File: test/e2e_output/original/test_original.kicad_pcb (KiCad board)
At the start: 2 copper layers, 3 parts, among them U1 CP_Radial_D25.0mm_P10.00mm_Sn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, U2 R_Axial_DIN0207_L6.3mm_D2.5mm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, U3 R_Axial_DIN0207_L6.3mm_D2.5mm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

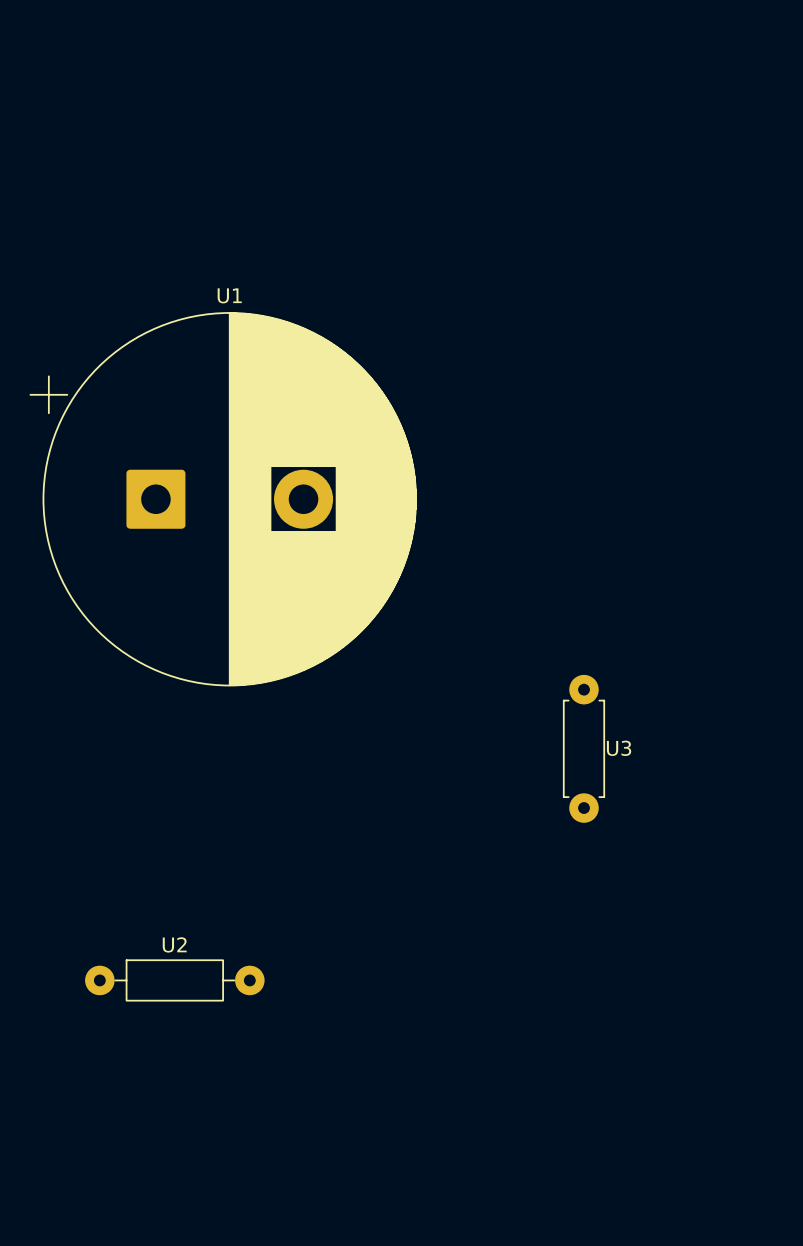
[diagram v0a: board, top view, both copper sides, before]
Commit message: fix: schematic router - pin_map mapping + rotation formula alignment
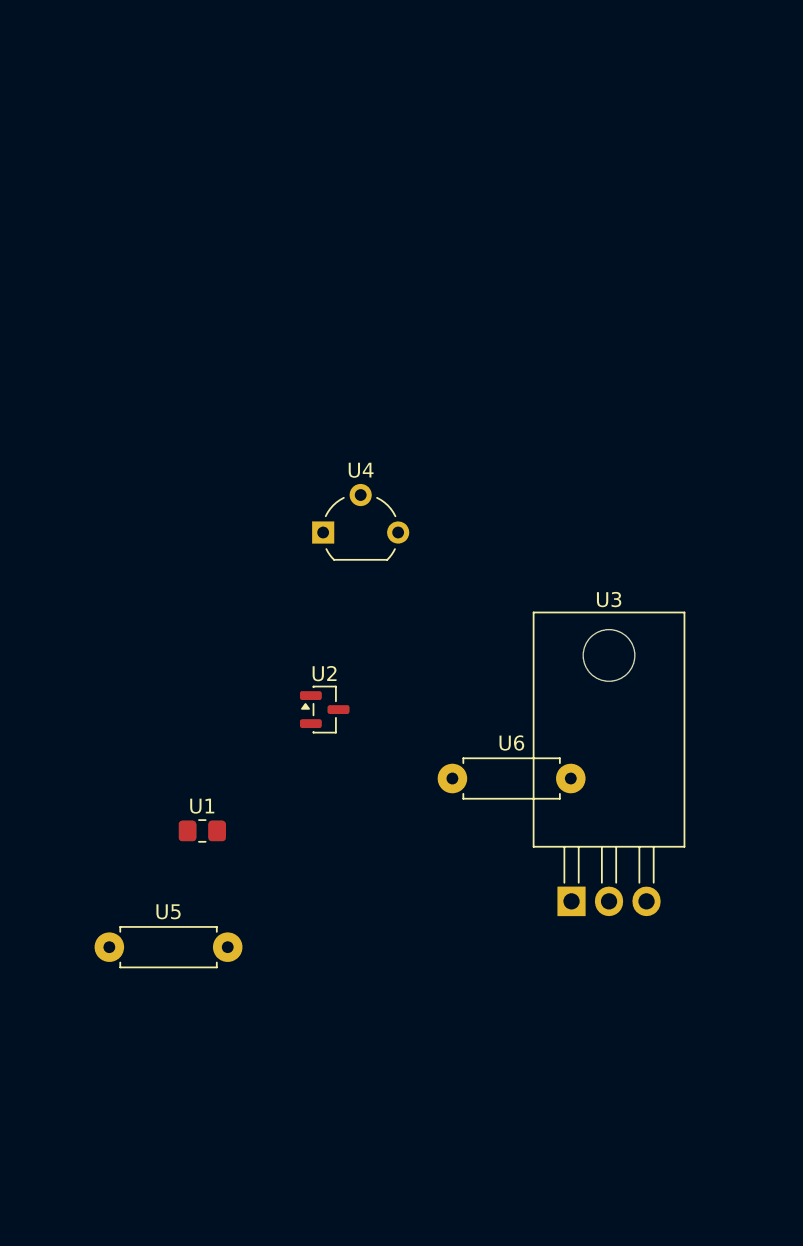
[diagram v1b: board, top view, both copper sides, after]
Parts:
- added U4: TO-92_Wide, RE_active:TO-92_Wide, F.Cu at (147.2, 91.0)
- added U5: R_Axial_DIN0207_L6.3mm_D2.5mm_P7.62mm_Horizontal, RE_passive_tht:R_Axial_DIN0207_L6.3mm_D2.5mm_P7.62mm_Horizontal, F.Cu at (132.9, 119.0)
- added U6: R_Axial_DIN0207_L6.3mm_D2.5mm_P7.62mm_Horizontal, RE_passive_tht:R_Axial_DIN0207_L6.3mm_D2.5mm_P7.62mm_Horizontal, F.Cu at (156.2, 107.6)
- U1: value CP_Radial_D25.0mm_P10.00mm_SnapIn -> R_0805_2012Metric_Pad1.20x1.40mm_HandSolder; footprint 00_basic:CP_Radial_D25.0mm_P10.00mm_SnapIn -> 00_basic:R_0805_2012Metric_Pad1.20x1.40mm_HandSolder
- U2: value R_Axial_DIN0207_L6.3mm_D2.5mm_P10.16mm_Horizontal -> SOT-23; footprint 00_basic:R_Axial_DIN0207_L6.3mm_D2.5mm_P10.16mm_Horizontal -> RE_active:SOT-23
- U3: value R_Axial_DIN0207_L6.3mm_D2.5mm_P7.62mm_Horizontal -> TO-220-3_Horizontal_TabDown; footprint 00_basic:R_Axial_DIN0207_L6.3mm_D2.5mm_P7.62mm_Horizontal -> RE_active:TO-220-3_Horizontal_TabDown
- moved U2 23.8 mm to (147.3, 103.0)
- moved U1 22.7 mm to (139.0, 111.2)
- moved U3 14.2 mm to (164.1, 115.9), turned to 0 degrees

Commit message: backup
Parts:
- added U7: CP_Radial_D30.0mm_P10.00mm_SnapIn, RE_passive_tht:CP_Radial_D30.0mm_P10.00mm_SnapIn, F.Cu at (157.5, 74.2)
- moved U1 16.8 mm to (139.0, 128.0)
- moved U4 16.8 mm to (147.2, 107.7)
- moved U3 16.8 mm to (164.1, 132.7)
- moved U2 16.8 mm to (147.3, 119.7)
- moved U6 16.8 mm to (156.2, 124.4)
- moved U5 16.8 mm to (132.9, 135.8)
